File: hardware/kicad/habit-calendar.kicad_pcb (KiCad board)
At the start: 2 copper layers, 100 x 100 mm, 80 parts, among them J1 Conn_01x01, J10 Conn_01x01, J12 Conn_01x01, J13 Conn_01x01, J15 Conn_01x01, J16 Conn_01x01, J17 Conn_01x01, J18 Conn_01x01, J19 Conn_01x01, J2 Conn_01x01, J20 Conn_01x01, J21 Conn_01x01, J22 Conn_01x01, J23 Conn_01x01, J24 Conn_01x01, J25 Conn_01x01, J3 Conn_01x01, J30 Conn_01x06, J4 Conn_01x06, J6 Conn_01x01, J7 Conn_01x01, J8 Conn_01x01, J9 Conn_01x01, SW1 TS-1187A-B-A-B, SW10 TS-1187A-B-A-B, SW11 TS-1187A-B-A-B, SW12 TS-1187A-B-A-B, SW2 TS-1187A-B-A-B, SW3 TS-1187A-B-A-B, SW4 TS-1187A-B-A-B, SW5 TS-1187A-B-A-B, SW6 TS-1187A-B-A-B, SW7 TS-1187A-B-A-B, SW8 TS-1187A-B-A-B, SW9 TS-1187A-B-A-B, U1 PY32F002AF15P6TU

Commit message: One micor ready. About to double the board.
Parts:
- removed J3: Conn_01x01, Connector_PinHeader_2.54mm:PinHeader_1x01_P2.54mm_Vertical
- added H1: MountingHole, MountingHole:MountingHole_2.2mm_M2, F.Cu at (115.1, 45.4)
- added H2: MountingHole, MountingHole:MountingHole_2.2mm_M2, F.Cu at (108.8, 86.7)
- added H3: MountingHole, MountingHole:MountingHole_2.2mm_M2, F.Cu at (206.4, 45.4)
- added H4: MountingHole, MountingHole:MountingHole_2.2mm_M2, F.Cu at (215.2, 88.1)
- added J11: Conn_01x01, Connector_PinHeader_2.54mm:PinHeader_1x01_P2.54mm_Vertical, F.Cu at (133.8, 45.6)
- added J14: Conn_01x01, Connector_PinHeader_2.54mm:PinHeader_1x01_P2.54mm_Vertical, F.Cu at (133.7, 57.5)
- added J26: Conn_01x01, Connector_PinHeader_2.54mm:PinHeader_1x01_P2.54mm_Vertical, F.Cu at (165.9, 70.0)
- added J27: Conn_01x01, Connector_PinHeader_2.54mm:PinHeader_1x01_P2.54mm_Vertical, F.Cu at (165.9, 82.5)
- added J29: Conn_01x01, Connector_PinHeader_2.54mm:PinHeader_1x01_P2.54mm_Vertical, F.Cu at (197.8, 57.4)
- added J31: Conn_01x01, Connector_PinHeader_2.54mm:PinHeader_1x01_P2.54mm_Vertical, F.Cu at (197.8, 82.5)
- added J5: Conn_01x10, Connector_PinHeader_2.54mm:PinHeader_1x10_P2.54mm_Vertical, F.Cu at (151.1, 88.1)
- added R20: 0 ohm, Resistor_SMD:R_0402_1005Metric, F.Cu at (139.4, 47.5)
- added R21: 0 ohm, Resistor_SMD:R_0402_1005Metric, F.Cu at (142.7, 47.5)
- added R22: 0 ohm, Resistor_SMD:R_0402_1005Metric, F.Cu at (145.0, 47.5)
- added R23: 0 ohm, Resistor_SMD:R_0402_1005Metric, F.Cu at (148.1, 47.5)
- J30: value Conn_01x06 -> Conn_01x01; footprint Connector_PinHeader_2.54mm:PinHeader_1x06_P2.54mm_Vertical -> Connector_PinHeader_2.54mm:PinHeader_1x01_P2.54mm_Vertical
- J4: value Conn_01x06 -> Conn_01x10; footprint Connector_PinHeader_2.54mm:PinHeader_1x06_P2.54mm_Vertical -> Connector_PinHeader_2.54mm:PinHeader_1x10_P2.54mm_Vertical
- moved J21 58.8 mm to (133.7, 82.5)
- moved J30 49.8 mm to (197.8, 70.0), turned to 0 degrees
- moved J19 46.1 mm to (133.7, 70.0)
- moved J25 40.7 mm to (165.8, 57.5)
- moved J24 38.8 mm to (165.9, 45.6)
- moved J23 5.15 mm to (206.7, 88.2)
- moved J22 4.48 mm to (206.7, 40.9)
- moved C13 0.64 mm to (146.8, 59.2), turned to -90 degrees
- moved R16 0.58 mm to (146.8, 68.6), turned to -90 degrees
- moved J4 0.40 mm to (150.8, 40.9)
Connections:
- J12 pad 1: Net-(J12-Pad1) -> /SW8
- J16 pad 1: Net-(J16-Pad1) -> /SW9
- J19 pad 1: +5V -> Net-(LED3-Pad4)
- J20 pad 1: Net-(J20-Pad1) -> /SW12
- J21 pad 1: GND -> Net-(LED3-Pad2)
- J22 pad 1: Net-(LED1-Pad2) -> /WS2812b - Din
- J23 pad 1: Net-(LED12-Pad4) -> Net-(LED12-Pad2)
- J24 pad 1: +5V -> Net-(LED5-Pad4)
- J25 pad 1: GND -> Net-(LED6-Pad4)
- J30 pad 1: Net-(J30-Pad1) -> Net-(LED11-Pad4)
- J4 pad 6: +5V -> GND
- J9 pad 1: Net-(J9-Pad1) -> /SW6
- LED1 pad 2: Net-(LED1-Pad2) -> Net-(LED2-Pad4)
- LED1 pad 4: Net-(LED1-Pad4) -> /WS2812b - Din
- LED10 pad 2: Net-(LED10-Pad2) -> Net-(LED11-Pad4)
- LED11 pad 2: Net-(LED10-Pad4) -> Net-(LED12-Pad4)
- LED12 pad 2: Net-(LED11-Pad4) -> Net-(LED12-Pad2)
- LED2 pad 2: Net-(LED1-Pad4) -> Net-(LED3-Pad4)
- LED3 pad 2: Net-(LED2-Pad4) -> Net-(LED3-Pad2)
- LED4 pad 2: Net-(LED3-Pad4) -> Net-(LED4-Pad2)
- LED4 pad 4: Net-(LED4-Pad4) -> Net-(LED3-Pad2)
- LED5 pad 2: Net-(LED4-Pad4) -> Net-(LED5-Pad2)
- LED8 pad 4: Net-(LED8-Pad4) -> Net-(LED4-Pad2)
- LED9 pad 2: Net-(LED8-Pad4) -> Net-(LED10-Pad4)
- LED9 pad 4: Net-(LED10-Pad2) -> Net-(LED5-Pad2)
- R10 pad 1: Net-(J9-Pad1) -> /SW6
- R12 pad 1: Net-(J30-Pad2) -> Net-(R12-Pad1)
- R13 pad 1: Net-(J12-Pad1) -> /SW8
- R14 pad 1: Net-(J30-Pad1) -> Net-(R14-Pad1)
- R15 pad 1: Net-(J16-Pad1) -> /SW9
- R19 pad 1: Net-(J20-Pad1) -> /SW12
- R4 pad 1: Net-(J30-Pad4) -> Net-(R4-Pad1)
- R5 pad 1: Net-(J30-Pad3) -> Net-(R5-Pad1)
- SW12 pad 1: Net-(J20-Pad1) -> /SW12
- SW12 pad 2: Net-(J20-Pad1) -> /SW12
- SW6 pad 1: Net-(J9-Pad1) -> /SW6
- SW6 pad 2: Net-(J9-Pad1) -> /SW6
- SW8 pad 1: Net-(J12-Pad1) -> /SW8
- SW8 pad 2: Net-(J12-Pad1) -> /SW8
- SW9 pad 1: Net-(J16-Pad1) -> /SW9
- SW9 pad 2: Net-(J16-Pad1) -> /SW9
- U1 pad 11: Net-(J20-Pad1) -> /SW8
- U1 pad 14: Net-(J12-Pad1) -> /SW9
- U1 pad 15: Net-(J9-Pad1) -> /SW12
- U1 pad 7: Net-(J16-Pad1) -> /SW6
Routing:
- net +5V: track 0.00 -> 710.9 mm, vias 0 -> 2
- net GND: track 0.00 -> 127.6 mm, vias 0 -> 87
- net /WS2812b - Din: track 0.00 -> 85.7 mm
- net /SW12: track 0.00 -> 73.9 mm, vias 0 -> 2
- net /SW9: track 0.00 -> 71.2 mm, vias 0 -> 2
- net Net-(J18-Pad1): track 0.00 -> 54.0 mm, vias 0 -> 2
- net Net-(J17-Pad1): track 0.00 -> 50.6 mm, vias 0 -> 2
- net /SW8: track 0.00 -> 50.6 mm, vias 0 -> 4
- net Net-(LED4-Pad2): track 0.00 -> 50.2 mm, vias 0 -> 2
- net Net-(LED5-Pad2): track 0.00 -> 44.9 mm, vias 0 -> 2
- net Net-(J10-Pad1): track 0.00 -> 44.8 mm, vias 0 -> 4
- net /SW6: track 0.00 -> 44.2 mm, vias 0 -> 2
- net /PF1: track 0.00 -> 38.3 mm, vias 0 -> 4
- net Net-(R4-Pad1): track 0.00 -> 36.2 mm
- net Net-(J13-Pad1): track 0.00 -> 34.6 mm, vias 0 -> 2
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- added copper zone on F.Cu, net +5V
- added copper zone on B.Cu, net GND
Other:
- board size 100 x 100 mm -> 96 x 100 mm

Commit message: Got it. Just needs a logo.
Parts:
- added C1: 100nf, easyeda2kicadLocal:C0402, F.Cu at (129.3, 95.4)
- added C10: 100nf, easyeda2kicadLocal:C0402, F.Cu at (193.3, 107.2)
- added C11: 100nf, easyeda2kicadLocal:C0402, F.Cu at (193.3, 119.8)
- added C12: 100nf, easyeda2kicadLocal:C0402, F.Cu at (193.3, 132.2)
- added C13: 100nf, easyeda2kicadLocal:C0402, F.Cu at (146.8, 109.0)
- added C2: 100nf, easyeda2kicadLocal:C0402, F.Cu at (129.3, 107.3)
- added C3: 100nf, easyeda2kicadLocal:C0402, F.Cu at (129.2, 119.7)
- added C4: 100nf, easyeda2kicadLocal:C0402, F.Cu at (129.2, 132.2)
- added C5: 100nf, easyeda2kicadLocal:C0402, F.Cu at (161.4, 95.4)
- added C6: 100nf, easyeda2kicadLocal:C0402, F.Cu at (161.4, 107.2)
- added C7: 100nf, easyeda2kicadLocal:C0402, F.Cu at (161.5, 119.8)
- added C8: 100nf, easyeda2kicadLocal:C0402, F.Cu at (161.5, 132.3)
- added C9: 100nf, easyeda2kicadLocal:C0402, F.Cu at (193.3, 95.3)
- added J1: Conn_01x01, Connector_PinHeader_2.54mm:PinHeader_1x01_P2.54mm_Vertical, F.Cu at (156.8, 95.4)
- added J10: Conn_01x01, Connector_PinHeader_2.54mm:PinHeader_1x01_P2.54mm_Vertical, F.Cu at (124.8, 95.4)
- added J11: Conn_01x01, Connector_PinHeader_2.54mm:PinHeader_1x01_P2.54mm_Vertical, F.Cu at (133.8, 95.4)
- added J12: Conn_01x01, Connector_PinHeader_2.54mm:PinHeader_1x01_P2.54mm_Vertical, F.Cu at (124.8, 132.3)
- added J13: Conn_01x01, Connector_PinHeader_2.54mm:PinHeader_1x01_P2.54mm_Vertical, F.Cu at (124.8, 119.8)
- added J14: Conn_01x01, Connector_PinHeader_2.54mm:PinHeader_1x01_P2.54mm_Vertical, F.Cu at (133.7, 107.3)
- added J15: Conn_01x01, Connector_PinHeader_2.54mm:PinHeader_1x01_P2.54mm_Vertical, F.Cu at (154.8, 113.5)
- added J16: Conn_01x01, Connector_PinHeader_2.54mm:PinHeader_1x01_P2.54mm_Vertical, F.Cu at (188.8, 95.3)
- added J17: Conn_01x01, Connector_PinHeader_2.54mm:PinHeader_1x01_P2.54mm_Vertical, F.Cu at (188.8, 107.2)
- added J18: Conn_01x01, Connector_PinHeader_2.54mm:PinHeader_1x01_P2.54mm_Vertical, F.Cu at (188.7, 119.8)
- added J19: Conn_01x01, Connector_PinHeader_2.54mm:PinHeader_1x01_P2.54mm_Vertical, F.Cu at (133.7, 119.8)
- added J2: Conn_01x01, Connector_PinHeader_2.54mm:PinHeader_1x01_P2.54mm_Vertical, F.Cu at (156.8, 107.3)
- added J20: Conn_01x01, Connector_PinHeader_2.54mm:PinHeader_1x01_P2.54mm_Vertical, F.Cu at (188.8, 132.2)
- added J21: Conn_01x01, Connector_PinHeader_2.54mm:PinHeader_1x01_P2.54mm_Vertical, F.Cu at (133.7, 132.3)
- added J24: Conn_01x01, Connector_PinHeader_2.54mm:PinHeader_1x01_P2.54mm_Vertical, F.Cu at (165.9, 95.4)
- added J25: Conn_01x01, Connector_PinHeader_2.54mm:PinHeader_1x01_P2.54mm_Vertical, F.Cu at (165.9, 107.3)
- added J26: Conn_01x01, Connector_PinHeader_2.54mm:PinHeader_1x01_P2.54mm_Vertical, F.Cu at (166.0, 119.8)
- added J27: Conn_01x01, Connector_PinHeader_2.54mm:PinHeader_1x01_P2.54mm_Vertical, F.Cu at (165.9, 132.3)
- added J29: Conn_01x01, Connector_PinHeader_2.54mm:PinHeader_1x01_P2.54mm_Vertical, F.Cu at (197.8, 107.2)
- added J30: Conn_01x01, Connector_PinHeader_2.54mm:PinHeader_1x01_P2.54mm_Vertical, F.Cu at (197.8, 119.8)
- added J31: Conn_01x01, Connector_PinHeader_2.54mm:PinHeader_1x01_P2.54mm_Vertical, F.Cu at (197.8, 132.3)
- added J6: Conn_01x01, Connector_PinHeader_2.54mm:PinHeader_1x01_P2.54mm_Vertical, F.Cu at (156.8, 119.8)
- added J7: Conn_01x01, Connector_PinHeader_2.54mm:PinHeader_1x01_P2.54mm_Vertical, F.Cu at (156.8, 132.3)
- added J8: Conn_01x01, Connector_PinHeader_2.54mm:PinHeader_1x01_P2.54mm_Vertical, F.Cu at (137.0, 113.5)
- added J9: Conn_01x01, Connector_PinHeader_2.54mm:PinHeader_1x01_P2.54mm_Vertical, F.Cu at (124.8, 107.3)
- added LED1: XL-5050RGBC-WS2812B, easyeda2kicadLocal3:LED-SMD_4P-L5.0-W5.0-BL_XL-5050RGBC, F.Cu at (133.8, 95.4)
- added LED10: XL-5050RGBC-WS2812B, easyeda2kicadLocal3:LED-SMD_4P-L5.0-W5.0-BL_XL-5050RGBC, F.Cu at (197.8, 107.2)
- added LED11: XL-5050RGBC-WS2812B, easyeda2kicadLocal3:LED-SMD_4P-L5.0-W5.0-BL_XL-5050RGBC, F.Cu at (197.8, 119.8)
- added LED12: XL-5050RGBC-WS2812B, easyeda2kicadLocal3:LED-SMD_4P-L5.0-W5.0-BL_XL-5050RGBC, F.Cu at (197.8, 132.3)
- added LED2: XL-5050RGBC-WS2812B, easyeda2kicadLocal3:LED-SMD_4P-L5.0-W5.0-BL_XL-5050RGBC, F.Cu at (133.8, 107.3)
- added LED3: XL-5050RGBC-WS2812B, easyeda2kicadLocal3:LED-SMD_4P-L5.0-W5.0-BL_XL-5050RGBC, F.Cu at (133.7, 119.8)
- added LED4: XL-5050RGBC-WS2812B, easyeda2kicadLocal3:LED-SMD_4P-L5.0-W5.0-BL_XL-5050RGBC, F.Cu at (133.7, 132.3)
- added LED5: XL-5050RGBC-WS2812B, easyeda2kicadLocal3:LED-SMD_4P-L5.0-W5.0-BL_XL-5050RGBC, F.Cu at (165.9, 95.4)
- added LED6: XL-5050RGBC-WS2812B, easyeda2kicadLocal3:LED-SMD_4P-L5.0-W5.0-BL_XL-5050RGBC, F.Cu at (165.9, 107.3)
- added LED7: XL-5050RGBC-WS2812B, easyeda2kicadLocal3:LED-SMD_4P-L5.0-W5.0-BL_XL-5050RGBC, F.Cu at (166.0, 119.8)
- added LED8: XL-5050RGBC-WS2812B, easyeda2kicadLocal3:LED-SMD_4P-L5.0-W5.0-BL_XL-5050RGBC, F.Cu at (166.0, 132.3)
- added LED9: XL-5050RGBC-WS2812B, easyeda2kicadLocal3:LED-SMD_4P-L5.0-W5.0-BL_XL-5050RGBC, F.Cu at (197.8, 95.3)
- added R1: 10k, Resistor_SMD:R_0402_1005Metric, F.Cu at (152.4, 95.3)
- added R10: 10k, Resistor_SMD:R_0402_1005Metric, F.Cu at (120.3, 107.3)
- added R11: 10k, Resistor_SMD:R_0402_1005Metric, F.Cu at (120.3, 119.8)
- added R12: 0 ohm, Resistor_SMD:R_0402_1005Metric, F.Cu at (140.0, 118.0)
- added R13: 10k, Resistor_SMD:R_0402_1005Metric, F.Cu at (120.3, 132.3)
- added R14: 0 ohm, Resistor_SMD:R_0402_1005Metric, F.Cu at (140.0, 121.0)
- added R15: 10k, Resistor_SMD:R_0402_1005Metric, F.Cu at (184.3, 95.3)
- added R16: 10k, Resistor_SMD:R_0402_1005Metric, F.Cu at (146.8, 118.4)
- added R17: 10k, Resistor_SMD:R_0402_1005Metric, F.Cu at (184.3, 107.2)
- added R18: 10k, Resistor_SMD:R_0402_1005Metric, F.Cu at (184.3, 119.7)
- added R19: 10k, Resistor_SMD:R_0402_1005Metric, F.Cu at (184.3, 132.2)
- added R2: 10k, Resistor_SMD:R_0402_1005Metric, F.Cu at (152.4, 107.3)
- added R20: 0 ohm, Resistor_SMD:R_0402_1005Metric, F.Cu at (139.5, 97.3)
- added R21: 0 ohm, Resistor_SMD:R_0402_1005Metric, F.Cu at (142.8, 97.3)
- added R22: 0 ohm, Resistor_SMD:R_0402_1005Metric, F.Cu at (145.0, 97.3)
- added R23: 0 ohm, Resistor_SMD:R_0402_1005Metric, F.Cu at (148.1, 97.3)
- added R3: 10k, Resistor_SMD:R_0402_1005Metric, F.Cu at (152.4, 119.8)
- added R4: 0 ohm, Resistor_SMD:R_0402_1005Metric, F.Cu at (140.0, 106.0)
- added R5: 0 ohm, Resistor_SMD:R_0402_1005Metric, F.Cu at (140.0, 109.0)
- added R6: 10k, Resistor_SMD:R_0402_1005Metric, F.Cu at (152.4, 132.3)
- added R7: DNP, Resistor_SMD:R_0402_1005Metric, F.Cu at (140.0, 115.0)
- added R8: 10k, Resistor_SMD:R_0402_1005Metric, F.Cu at (140.0, 112.0)
- added R9: 10k, Resistor_SMD:R_0402_1005Metric, F.Cu at (120.3, 95.4)
- added SW1: TS-1187A-B-A-B, easyeda2kicad:SW-SMD_4P-L5.1-W5.1-P3.70-LS6.5-TL-2, F.Cu at (156.8, 95.4)
- added SW10: TS-1187A-B-A-B, easyeda2kicad:SW-SMD_4P-L5.1-W5.1-P3.70-LS6.5-TL-2, F.Cu at (188.8, 107.2)
- added SW11: TS-1187A-B-A-B, easyeda2kicad:SW-SMD_4P-L5.1-W5.1-P3.70-LS6.5-TL-2, F.Cu at (188.8, 119.7)
- added SW12: TS-1187A-B-A-B, easyeda2kicad:SW-SMD_4P-L5.1-W5.1-P3.70-LS6.5-TL-2, F.Cu at (188.8, 132.2)
- added SW2: TS-1187A-B-A-B, easyeda2kicad:SW-SMD_4P-L5.1-W5.1-P3.70-LS6.5-TL-2, F.Cu at (156.8, 107.3)
- added SW3: TS-1187A-B-A-B, easyeda2kicad:SW-SMD_4P-L5.1-W5.1-P3.70-LS6.5-TL-2, F.Cu at (156.8, 119.8)
- added SW4: TS-1187A-B-A-B, easyeda2kicad:SW-SMD_4P-L5.1-W5.1-P3.70-LS6.5-TL-2, F.Cu at (156.8, 132.3)
- added SW5: TS-1187A-B-A-B, easyeda2kicad:SW-SMD_4P-L5.1-W5.1-P3.70-LS6.5-TL-2, F.Cu at (124.8, 95.4)
- added SW6: TS-1187A-B-A-B, easyeda2kicad:SW-SMD_4P-L5.1-W5.1-P3.70-LS6.5-TL-2, F.Cu at (124.8, 107.3)
- added SW7: TS-1187A-B-A-B, easyeda2kicad:SW-SMD_4P-L5.1-W5.1-P3.70-LS6.5-TL-2, F.Cu at (124.8, 119.8)
- added SW8: TS-1187A-B-A-B, easyeda2kicad:SW-SMD_4P-L5.1-W5.1-P3.70-LS6.5-TL-2, F.Cu at (124.8, 132.3)
- added SW9: TS-1187A-B-A-B, easyeda2kicad:SW-SMD_4P-L5.1-W5.1-P3.70-LS6.5-TL-2, F.Cu at (188.8, 95.3)
- added U1: PY32F002AF15P6TU, easyeda2kicad:TSSOP-20_L6.5-W4.4-P0.65-LS6.4-BL, F.Cu at (146.6, 113.8)
- moved J23 49.8 mm to (206.7, 138.0)
- moved J5 49.8 mm to (150.8, 137.9)
- moved H2 46.2 mm to (115.4, 132.4)
- moved H4 45.2 mm to (206.0, 132.4)
- moved H3 0.43 mm to (206.0, 45.4)
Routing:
- net +5V: track 710.9 -> 1454.0 mm, vias 2 -> 4
- net GND: track 127.6 -> 244.6 mm, vias 87 -> 168
- net /SW12: track 73.9 -> 147.8 mm, vias 2 -> 4
- net /WS2812b - Din: track 85.7 -> 156.0 mm
- net /SW9: track 71.2 -> 133.3 mm, vias 2 -> 4
- net Net-(LED4-Pad2): track 50.2 -> 107.9 mm, vias 2 -> 4
- net Net-(J18-Pad1): track 54.0 -> 107.6 mm, vias 2 -> 4
- net Net-(J17-Pad1): track 50.6 -> 101.2 mm, vias 2 -> 4
- net /SW8: track 50.6 -> 101.2 mm, vias 4 -> 8
- net Net-(J10-Pad1): track 44.8 -> 94.6 mm, vias 4 -> 8
- net /SW6: track 44.2 -> 92.9 mm, vias 2 -> 4
- net Net-(LED5-Pad2): track 44.9 -> 89.8 mm, vias 2 -> 4
- net /PF1: track 38.3 -> 80.2 mm, vias 4 -> 8
- net /PF0: track 34.4 -> 71.7 mm, vias 2 -> 4
- net Net-(J13-Pad1): track 34.6 -> 71.5 mm, vias 2 -> 4
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- added copper zone on F.Cu, net GND

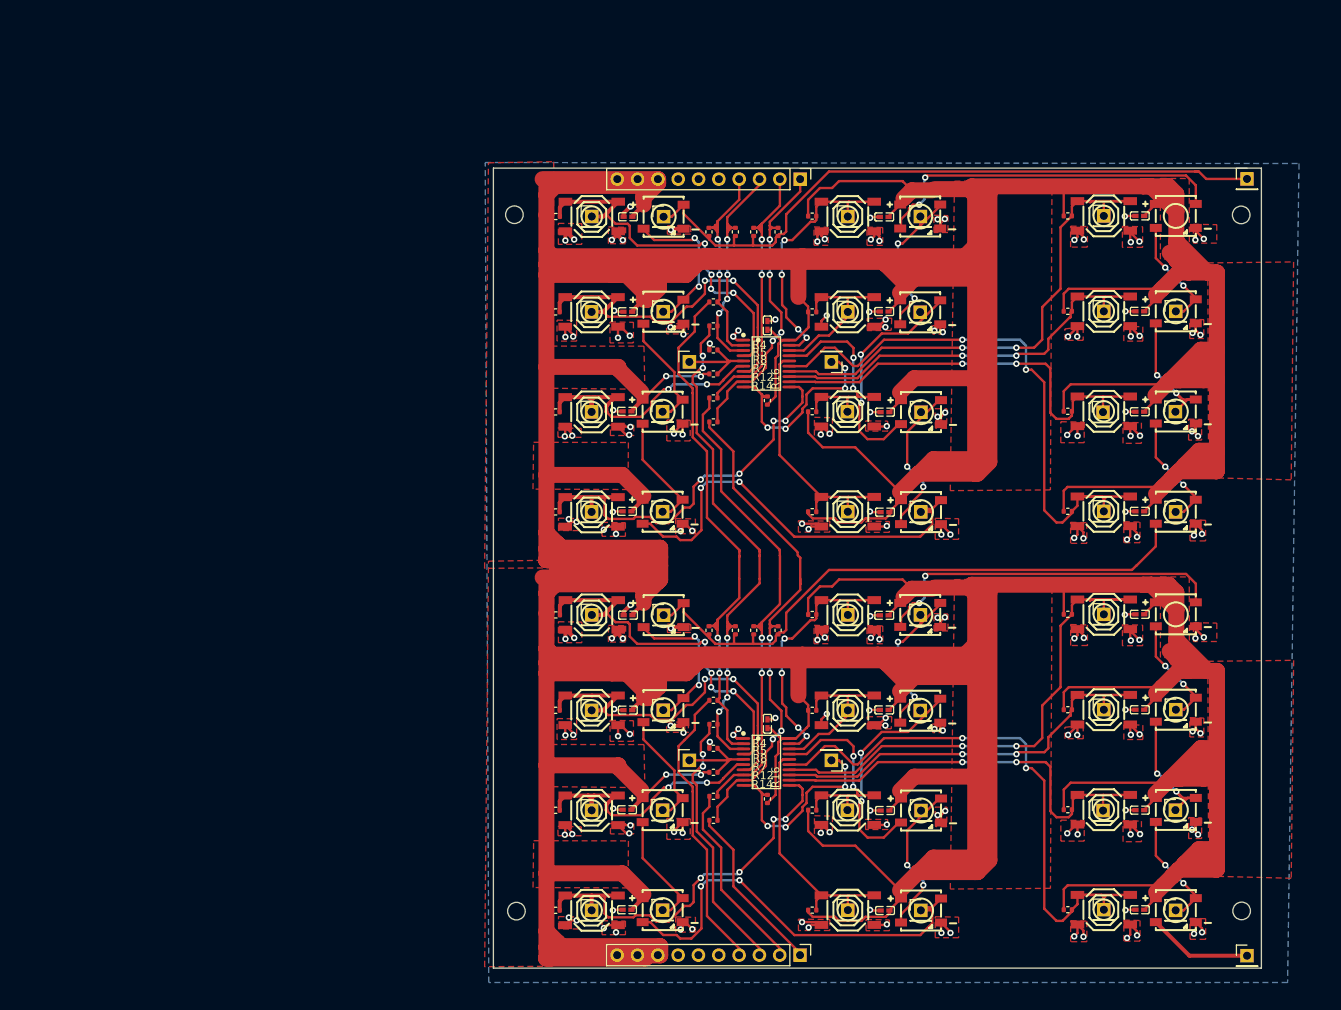
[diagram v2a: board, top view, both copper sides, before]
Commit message: small tweaks but still single board. might change up edge connector
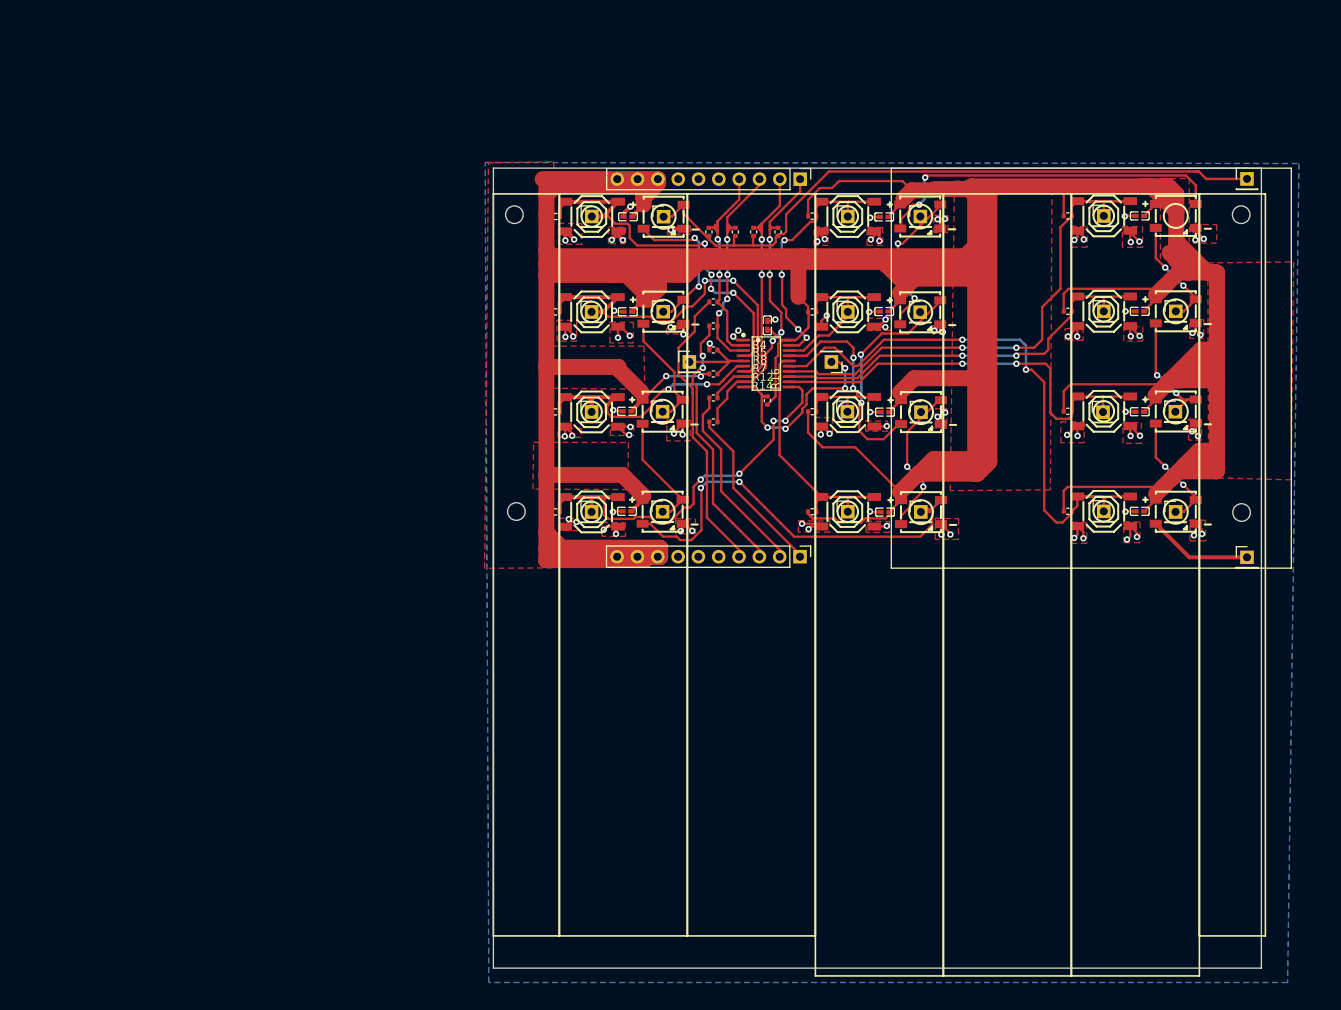
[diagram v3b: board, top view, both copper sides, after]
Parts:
- removed the C1 at (129.3, 95.4)
- removed the C10 at (193.3, 107.2)
- removed the C11 at (193.3, 119.8)
- removed the C12 at (193.3, 132.2)
- removed the C13 at (146.8, 109.0)
- removed the C2 at (129.3, 107.3)
- removed the C3 at (129.2, 119.7)
- removed the C4 at (129.2, 132.2)
- removed the C5 at (161.4, 95.4)
- removed the C6 at (161.4, 107.2)
- removed the C7 at (161.5, 119.8)
- removed the C8 at (161.5, 132.3)
- removed the C9 at (193.3, 95.3)
- removed the J1 at (156.8, 95.4)
- removed the J10 at (124.8, 95.4)
- removed the J11 at (133.8, 95.4)
- removed the J12 at (124.8, 132.3)
- removed the J13 at (124.8, 119.8)
- removed the J14 at (133.7, 107.3)
- removed the J15 at (154.8, 113.5)
- removed the J16 at (188.8, 95.3)
- removed the J17 at (188.8, 107.2)
- removed the J18 at (188.7, 119.8)
- removed the J19 at (133.7, 119.8)
- removed the J2 at (156.8, 107.3)
- removed the J20 at (188.8, 132.2)
- removed the J21 at (133.7, 132.3)
- removed the J24 at (165.9, 95.4)
- removed the J25 at (165.9, 107.3)
- removed the J26 at (166.0, 119.8)
- removed the J27 at (165.9, 132.3)
- removed the J29 at (197.8, 107.2)
- removed the J30 at (197.8, 119.8)
- removed the J31 at (197.8, 132.3)
- removed the J6 at (156.8, 119.8)
- removed the J7 at (156.8, 132.3)
- removed the J8 at (137.0, 113.5)
- removed the J9 at (124.8, 107.3)
- removed the LED1 at (133.8, 95.4)
- removed the LED10 at (197.8, 107.2)
- removed the LED11 at (197.8, 119.8)
- removed the LED12 at (197.8, 132.3)
- removed the LED2 at (133.8, 107.3)
- removed the LED3 at (133.7, 119.8)
- removed the LED4 at (133.7, 132.3)
- removed the LED5 at (165.9, 95.4)
- removed the LED6 at (165.9, 107.3)
- removed the LED7 at (166.0, 119.8)
- removed the LED8 at (166.0, 132.3)
- removed the LED9 at (197.8, 95.3)
- removed the R1 at (152.4, 95.3)
- removed the R10 at (120.3, 107.3)
- removed the R11 at (120.3, 119.8)
- removed the R12 at (140.0, 118.0)
- removed the R13 at (120.3, 132.3)
- removed the R14 at (140.0, 121.0)
- removed the R15 at (184.3, 95.3)
- removed the R16 at (146.8, 118.4)
- removed the R17 at (184.3, 107.2)
- removed the R18 at (184.3, 119.7)
- removed the R19 at (184.3, 132.2)
- removed the R2 at (152.4, 107.3)
- removed the R20 at (139.5, 97.3)
- removed the R21 at (142.8, 97.3)
- removed the R22 at (145.0, 97.3)
- removed the R23 at (148.1, 97.3)
- removed the R3 at (152.4, 119.8)
- removed the R4 at (140.0, 106.0)
- removed the R5 at (140.0, 109.0)
- removed the R6 at (152.4, 132.3)
- removed the R7 at (140.0, 115.0)
- removed the R8 at (140.0, 112.0)
- removed the R9 at (120.3, 95.4)
- removed the SW1 at (156.8, 95.4)
- removed the SW10 at (188.8, 107.2)
- removed the SW11 at (188.8, 119.7)
- removed the SW12 at (188.8, 132.2)
- removed the SW2 at (156.8, 107.3)
- removed the SW3 at (156.8, 119.8)
- removed the SW4 at (156.8, 132.3)
- removed the SW5 at (124.8, 95.4)
- removed the SW6 at (124.8, 107.3)
- removed the SW7 at (124.8, 119.8)
- removed the SW8 at (124.8, 132.3)
- removed the SW9 at (188.8, 95.3)
- removed the U1 at (146.6, 113.8)
- moved H2 50.0 mm to (115.4, 82.5)
- moved J5 49.8 mm to (150.8, 88.1)
- moved H4 49.8 mm to (206.0, 82.6)
- moved J23 49.8 mm to (206.7, 88.2)
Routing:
- net +5V: track 1454.0 -> 708.2 mm, vias 4 -> 2
- net GND: track 244.6 -> 122.3 mm, vias 168 -> 84
- net /SW12: track 147.8 -> 73.9 mm, vias 4 -> 2
- net /WS2812b - Din: track 156.0 -> 85.7 mm
- net /SW9: track 133.3 -> 66.6 mm, vias 4 -> 2
- net Net-(LED4-Pad2): track 107.9 -> 54.0 mm, vias 4 -> 2
- net Net-(J18-Pad1): track 107.6 -> 53.8 mm, vias 4 -> 2
- net Net-(J17-Pad1): track 101.2 -> 50.6 mm, vias 4 -> 2
- net /SW8: track 101.2 -> 50.6 mm, vias 8 -> 4
- net Net-(J10-Pad1): track 94.6 -> 47.3 mm, vias 8 -> 4
- net /SW6: track 92.9 -> 46.4 mm, vias 4 -> 2
- net Net-(LED5-Pad2): track 89.8 -> 44.9 mm, vias 4 -> 2
- net /PF1: track 80.2 -> 38.3 mm, vias 8 -> 4
- net /PF0: track 71.7 -> 34.4 mm, vias 4 -> 2
- net Net-(R4-Pad1): track 72.0 -> 36.1 mm
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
